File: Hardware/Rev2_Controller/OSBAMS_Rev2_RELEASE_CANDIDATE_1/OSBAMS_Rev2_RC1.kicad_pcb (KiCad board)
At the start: 4 copper layers, 100 x 90 mm, 142 parts, among them J1 12V_IN, J2 ESTOP, J3 ARM, J4 K1_COIL, J5 SHUNT_KELVIN, J6 PACK_SENSE, J7 TEMP_PROBE, J8 USB-C HOST, J9 SWD, Q1 IRLML0060, SW1 RESET, U1 STM32L476RGT6, U10 USBLC6-2SC6, U2 INA228, U3 LMR14006Y, U4 VO610A-1, U5 VO610A-1, U6 CP2102N, U7 ISO7721, U9 USBLC6-2SC6

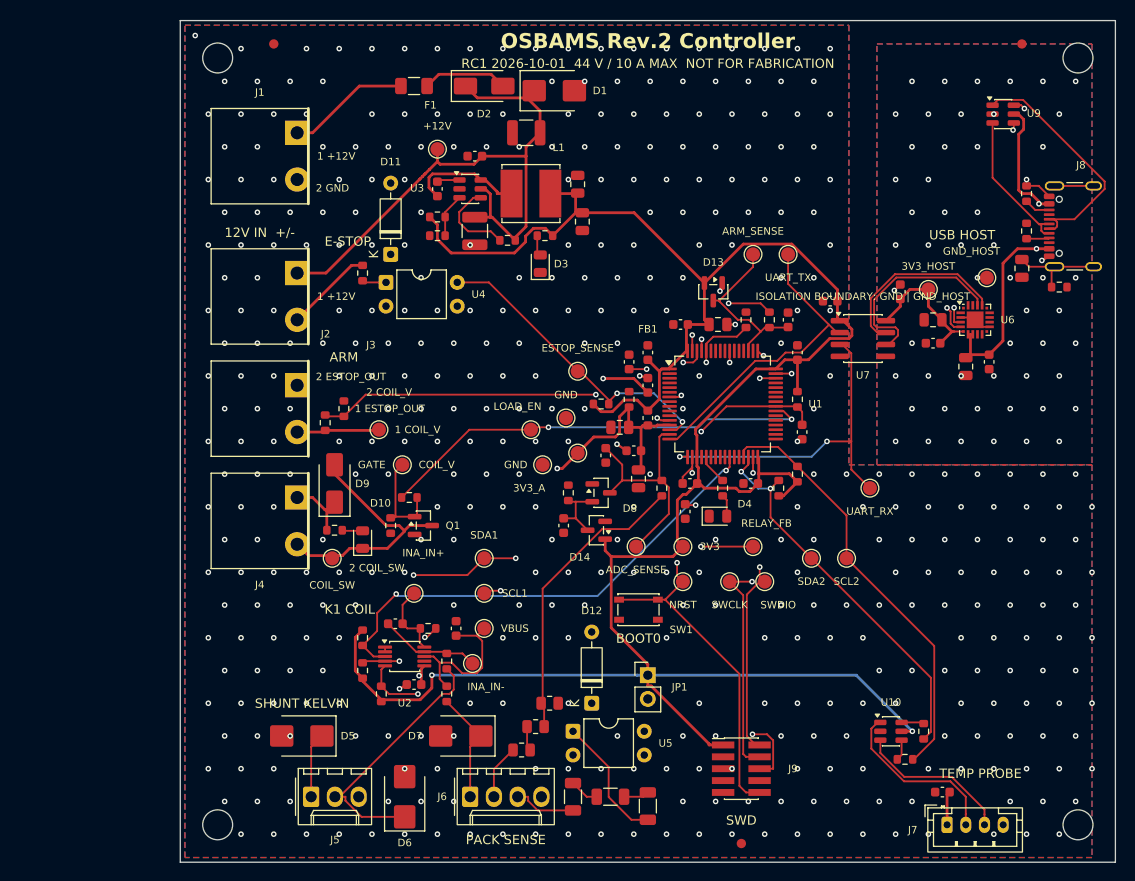
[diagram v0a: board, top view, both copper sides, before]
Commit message: RC1: EB21A-02-C footprint verified against the Adam Tech drawing (rev B); J1-J4 re-placed, board re-routed
Hole 1.30 mm, body 10.6 x 8.5 mm, wire entry toward the board edge; VERIFY_MECHANICAL_DRAWING removed
for this part only. ERC 0; DRC: 0 electrical, 4 silkscreen warnings, 0 unconnected.

Co-Authored-By: Claude Sonnet 5.5 <noreply@anthropic.com>
Claude-Session: https://claude.ai/code/session_01HV1TCrYnLTcNjmYdFqCPLo
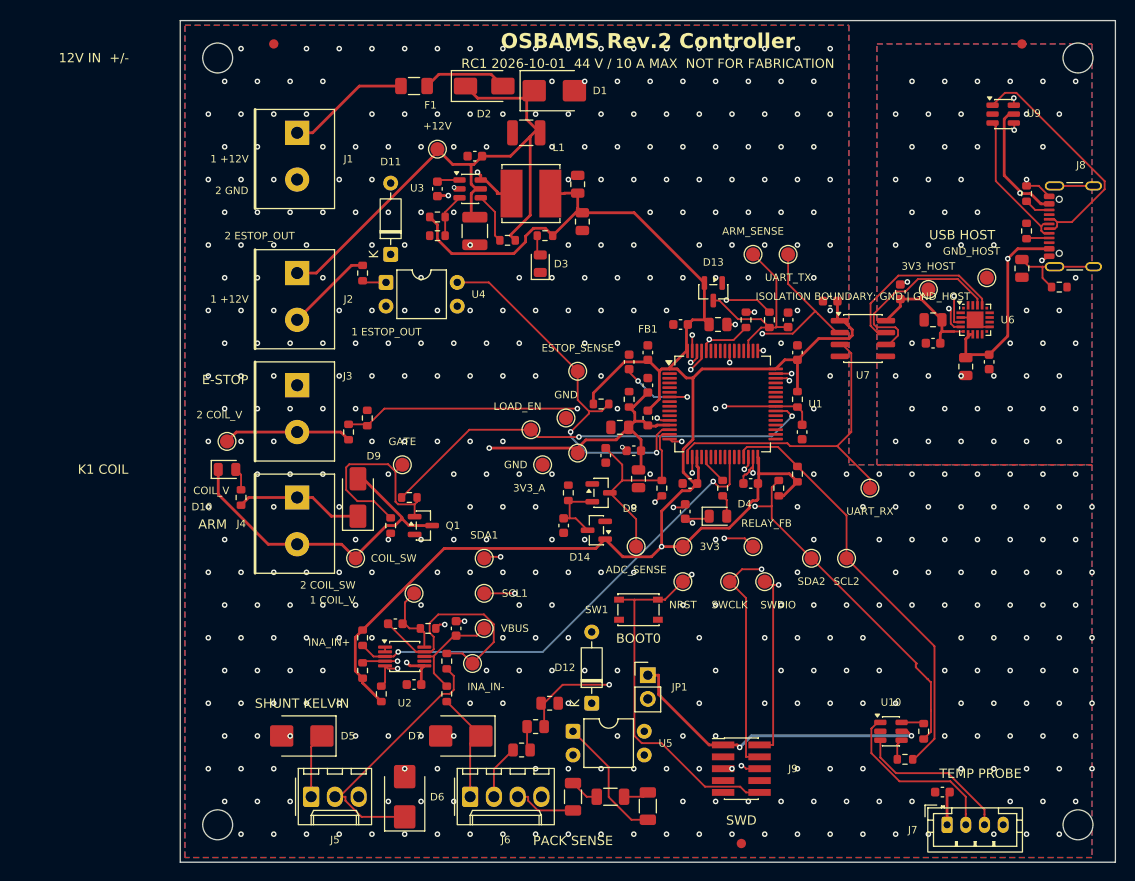
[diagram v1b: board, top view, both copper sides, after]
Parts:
- J1, J2, J3, J4: footprint OSBAMS_Rev2:EB21A-02-C_PROVISIONAL -> OSBAMS_Rev2:EB21A-02-C
- moved D10 16.3 mm to (105.0, 108.0), turned to 0 degrees
- moved TP16 16.3 mm to (105.0, 105.0)
- moved R23 10.6 mm to (106.5, 111.0), turned to 90 degrees
- moved D9 2.92 mm to (119.0, 111.0)
- moved R30 2.69 mm to (118.0, 104.0)
- moved R31 2.69 mm to (120.0, 102.5)
- moved TP15 2.50 mm to (118.8, 117.5)
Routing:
- net INA_INN: track 10.8 -> 25.2 mm
- net +3V3: track 272.4 -> 259.7 mm, vias 2 -> 3
- net GATE: track 10.6 -> 22.7 mm
- net COIL_V: track 22.9 -> 34.4 mm
- net 3V3_A: track 70.5 -> 61.7 mm, vias 3 -> 2
- net COIL_SW: track 28.5 -> 37.0 mm
- net NRST: track 61.7 -> 68.6 mm
- net INA_VBUS: track 17.0 -> 11.4 mm
- net ESTOP_SENSE: track 43.8 -> 49.0 mm
- net SCL1: track 63.8 -> 58.7 mm
- net SDA1: track 58.7 -> 53.9 mm, vias 4 -> 3
- net UART_TX_MCU: track 32.9 -> 37.5 mm, vias 0 -> 2
- net BUCK_EN: track 9.19 -> 5.39 mm
- net VBUS_USB: track 39.3 -> 42.8 mm
- net ARM_SENSE: track 18.7 -> 22.0 mm
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
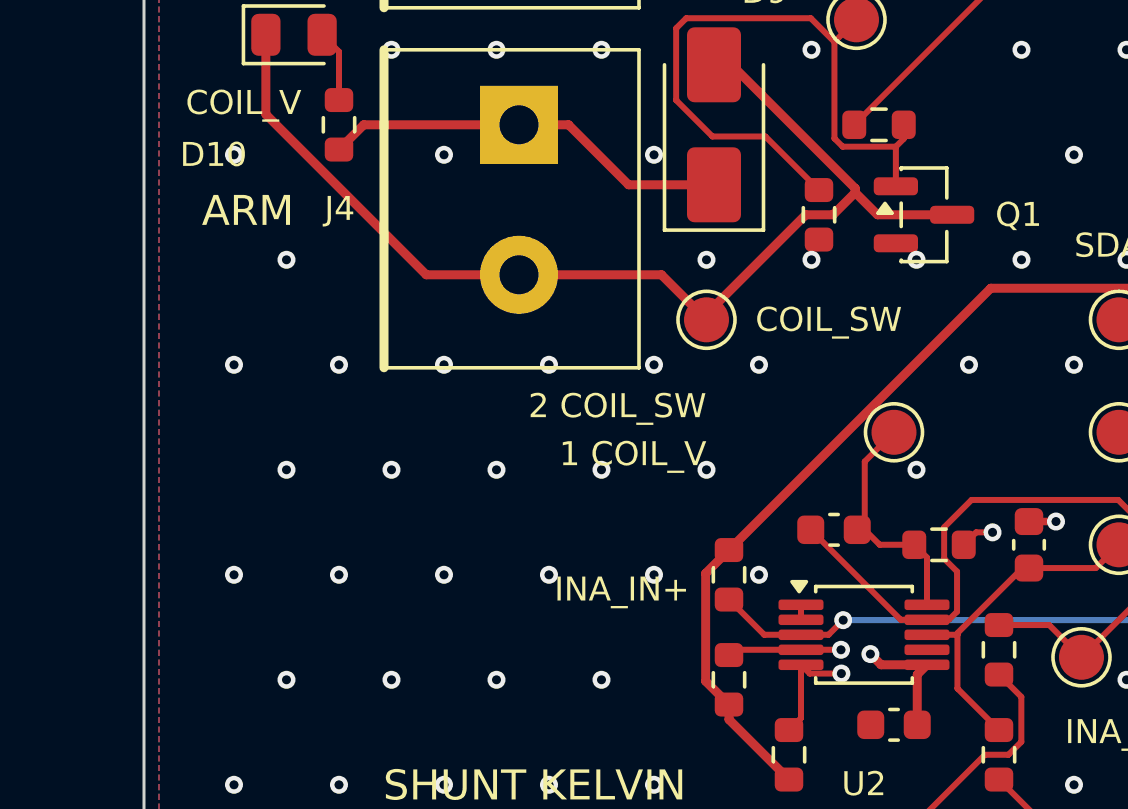
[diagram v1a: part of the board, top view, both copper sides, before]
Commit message: RC1: reconcile user-relayed manufacturer data (USER_RELAYED_MANUFACTURER)
- audit report MANUFACTURER_DATA_RECONCILIATION.md; INA228/STM32/IRLML0060/LMR14006Y/CP2102N/VO610A/TC74 pin maps match the relayed data
- ISO7721 pin-direction conflict left unresolved (needs the TI pin diagram); CP2102N VBUS reference connection open
- LMR14006Y: 95 ns TON_MIN analysis (15 V marginal, 24.4 V below TON_MIN); 1.5SMBJ48A vs INA228 85 V clamp-vs-current analysis
- firmware: INA228 IMAX 30 A -> 20 A (SHUNT_CAL 1250) + test
- fix: TC74 probe PCB had been left unrouted by the schematic step; re-routed, DRC 0; schematic step no longer rebuilds it

Co-Authored-By: Claude Sonnet 5.5 <noreply@anthropic.com>
Claude-Session: https://claude.ai/code/session_01HV1TCrYnLTcNjmYdFqCPLo
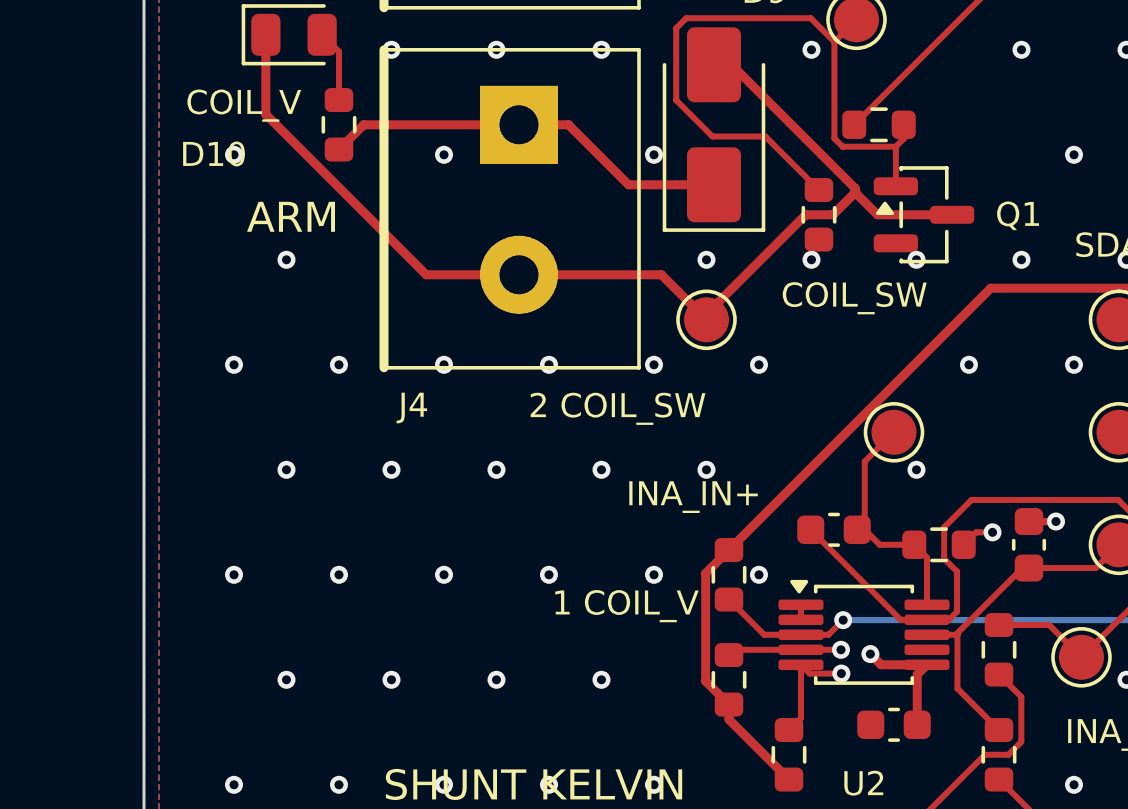
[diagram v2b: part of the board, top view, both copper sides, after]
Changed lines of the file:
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@@
 			)
 		)
-		(property "Evidence" "UNVERIFIED"
+		(property "Evidence" "USER_RELAYED_MANUFACTURER"
 			(at 0 0 0)
 			(layer "F.Fab")
@@
 		(tags "EB21A terminal block 5.00mm")
 		(property "Reference" "J4"
-			(at -5.975001 2.8 0)
+			(at -3.5125 9.360142 0)
 			(layer "F.SilkS")
 			(effects
@@
 			)
 		)
-		(property "Evidence" "UNVERIFIED"
+		(property "Evidence" "USER_RELAYED_MANUFACTURER"
 			(at 0 0 0)
 			(layer "F.Fab")
@@
 			)
 		)
-		(property "Evidence" "UNVERIFIED"
+		(property "Evidence" "USER_RELAYED_MANUFACTURER"
 			(at 0 0 0)
 			(layer "F.Fab")
@@
 			)
 		)
-		(property "Evidence" "USER_RELAYED_MANUFACTURER"
+		(property "Evidence" "UNVERIFIED"
 			(at 0 0 0)
 			(layer "F.Fab")
@@
 	)
 	(gr_text "INA_IN+"
-		(at 115.928383 126.4875 0)
+		(at 118.3225 123.310991 0)
 		(layer "F.SilkS")
 		(effects
@@
 	)
 	(gr_text "COIL_SW"
-		(at 122.825 117.5 0)
+		(at 123.6775 116.689008 0)
 		(layer "F.SilkS")
 		(effects
@@
 		)
 	)
-	(gr_text "2 COIL_SW"
-		(at 118.75 120.375 0)
+	(gr_text "1 COIL_V"
+		(at 118.49974 126.9525 0)
 		(layer "F.SilkS")
 		(effects
@@
 		)
 	)
-	(gr_text "1 COIL_V"
-		(at 118.75 121.975 0)
+	(gr_text "2 COIL_SW"
+		(at 118.75 120.375 0)
 		(layer "F.SilkS")
 		(effects
@@
 	)
 	(gr_text "ARM"
-		(at 105 113.875 0)
+		(at 106.5 114.104999 0)
 		(layer "F.SilkS")
 		(effects

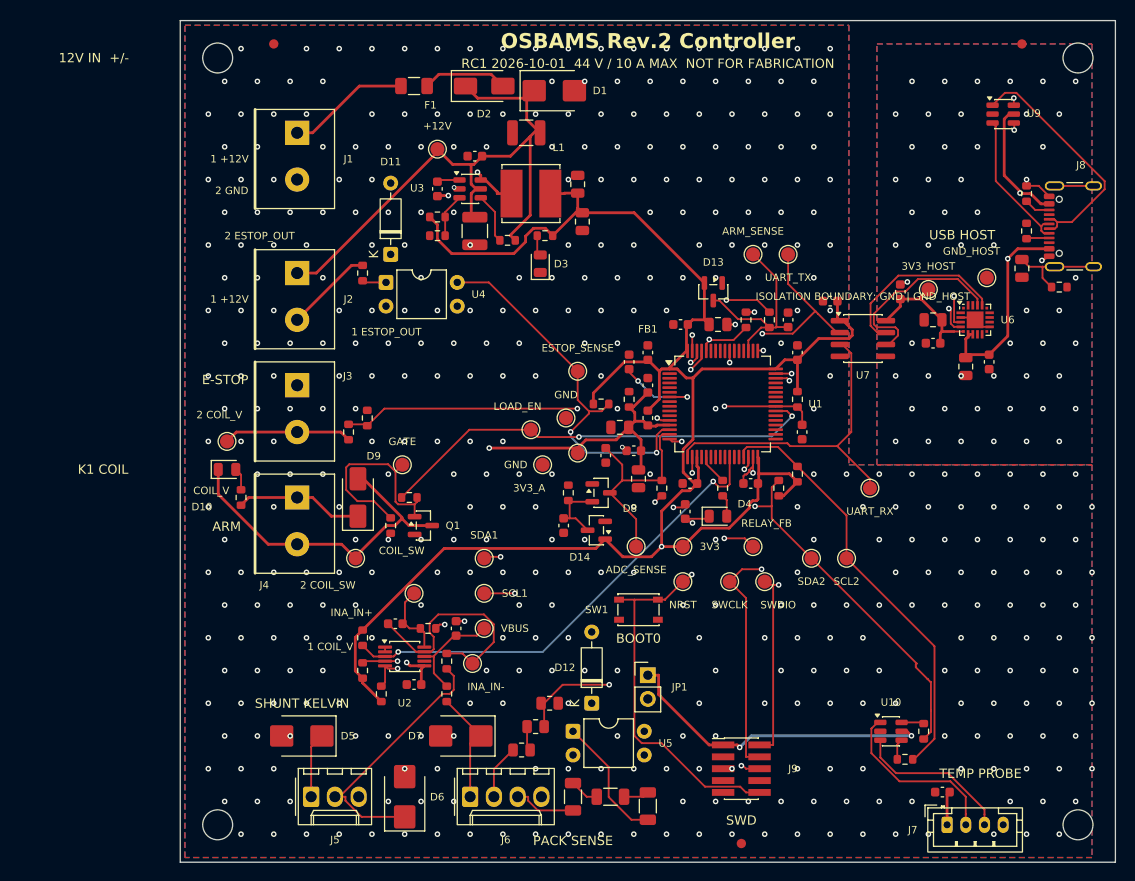
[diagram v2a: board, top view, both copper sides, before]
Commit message: RC1.1: ISO7721 pinout fix, CP2102N VBUS divider/RSTb pull-up/VDD bypass, datasheets read locally
- ISO7721 symbol corrected to the TI D/DWV table (2 OUTA, 3 INB, 6 OUTB, 7 INA); UART nets reassigned and re-routed
- CP2102N: VBUS 22.1k/47.5k divider (R38/R39), 1k RSTb pull-up (R40), VDD bypass 4.7uF (C22) per the datasheet
- ISO7721, CP2102N, SRN6045TA datasheets committed as evidence and marked VERIFIED_LOCAL; SRN6045TA-100M inductor closed
- isolation check script/report (3.0 mm in the ISO7721 area, 0.25 mm elsewhere); docs corrected (netclass clearances)
- board re-placed and re-routed: ERC 0, DRC 0 electrical (3 silkscreen warnings), netlist 0 mismatches

Co-Authored-By: Claude Sonnet 5.5 <noreply@anthropic.com>
Claude-Session: https://claude.ai/code/session_01HV1TCrYnLTcNjmYdFqCPLo
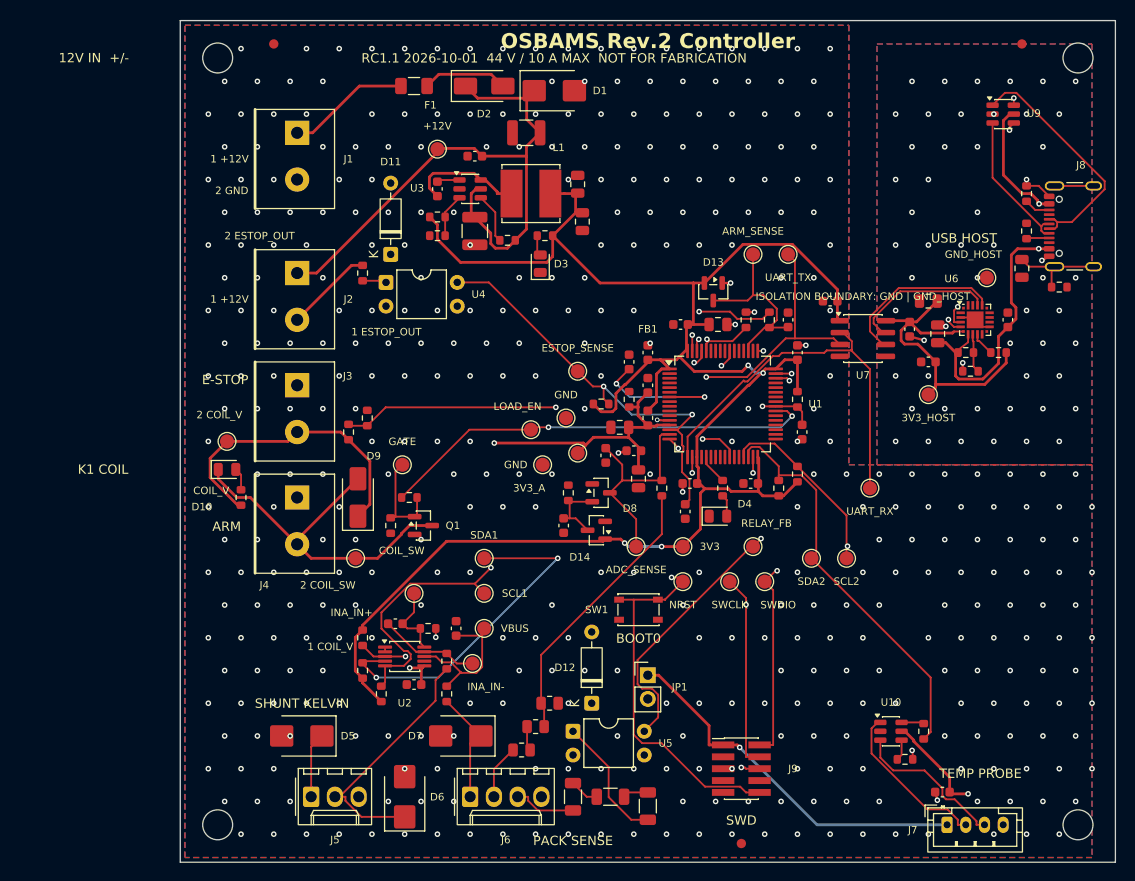
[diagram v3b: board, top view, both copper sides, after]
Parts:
- added R38: 22.1k, Resistor_SMD:R_0603_1608Metric, F.Cu at (184.0, 95.5)
- added R39: 47.5k, Resistor_SMD:R_0603_1608Metric, F.Cu at (184.5, 97.5)
- added R40: 1k, Resistor_SMD:R_0603_1608Metric, F.Cu at (187.5, 95.5)
- C22: value 1uF -> 4.7uF
- moved TP27 11.2 mm to (180.0, 100.0)
- moved C21 4.92 mm to (188.5, 92.0), turned to 90 degrees
- moved C20 4.61 mm to (181.0, 93.5), turned to 90 degrees
- moved C25 4.12 mm to (178.0, 93.0), turned to -90 degrees
- moved C22 2.06 mm to (180.0, 90.0)
- moved C23 2.06 mm to (180.0, 96.5)
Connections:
- U6 pad 8: VBUS_USB -> CP_VBUS_SENSE
- U6 pad 9: (no net) -> CP_RSTB
- U7 pad 2: UART_TX_MCU -> UART_RX_MCU
- U7 pad 3: UART_RX_MCU -> UART_TX_MCU
- U7 pad 6: UART_TX_HOST -> UART_RX_HOST
- U7 pad 7: UART_RX_HOST -> UART_TX_HOST
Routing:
- net 3V3_HOST: track 14.5 -> 33.2 mm
- net INA_INN: track 25.2 -> 10.8 mm
- net SDA1: track 53.9 -> 68.3 mm
- net GATE: track 22.7 -> 10.6 mm
- net +3V3: track 259.7 -> 271.7 mm, vias 3 -> 6
- net NRST: track 68.6 -> 76.5 mm
- net UART_RX_MCU: track 35.3 -> 41.8 mm
- net COIL_V: track 34.4 -> 39.6 mm
- net INA_VBUS: track 11.4 -> 16.3 mm
- net VBUS_USB: track 42.8 -> 47.7 mm
- net UART_TX_HOST: track 20.4 -> 15.6 mm
- net CP_VBUS_SENSE: track 0.00 -> 4.19 mm
- net ESTOP_SENSE: track 49.0 -> 45.0 mm, vias 3 -> 2
- net GND: track 18.5 -> 14.9 mm, vias 417 -> 404
- net RELAY_FB: track 51.7 -> 48.4 mm
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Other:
- board text added: "RC1.1 2026-10-01 44 V / 10 A MAX NOT FOR FABRICATION"
- board text removed: "RC1 2026-10-01 44 V / 10 A MAX NOT FOR FABRICATION"

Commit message: RC1.2: pack-sense surge resistors, isolation/clearance rules, buck envelope, evidence classification, no shipped Gerbers
- R41 47R (PACK_INA) and R42/R43 10R (Kelvin lines) upstream of the 1.5SMBJ48A diodes; credible-transient analysis with simulation (PASS)
- custom DRC rules: host-to-controller >= 1.0 mm on every layer, INA228 fine-pitch exemption; pack-level class 0.2 mm (IPC-2221B B4 basis)
- isolation audit per layer with coordinates; XDR 12.0 V / max continuous input 14.4 V; IRLML0060 margin estimate + mandatory first-article checks
- board re-routed: ERC 0, DRC 0, unconnected 0, netlist 0 mismatches (403 pads); silkscreen warnings fixed
- script-generated Gerbers/drills removed from the package; BOM adds qty for 5 boards and MPN suffix status; new evidence-risk, connector-check and pre-PCBWay checklist documents

Co-Authored-By: Claude Sonnet 5.5 <noreply@anthropic.com>
Claude-Session: https://claude.ai/code/session_01HV1TCrYnLTcNjmYdFqCPLo
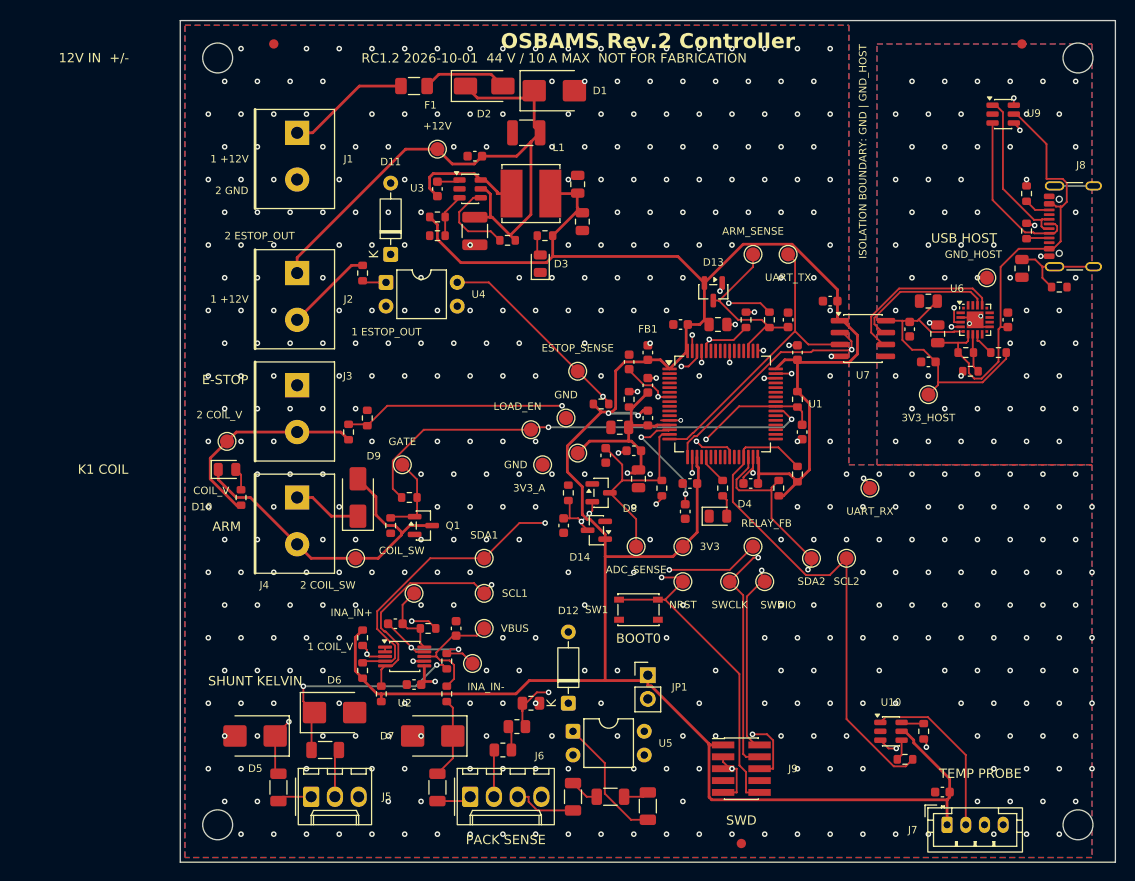
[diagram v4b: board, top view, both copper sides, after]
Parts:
- added R41: 47, Resistor_SMD:R_1206_3216Metric, F.Cu at (127.5, 142.0)
- added R42: 10, Resistor_SMD:R_1206_3216Metric, F.Cu at (110.5, 142.0)
- added R43: 10, Resistor_SMD:R_1206_3216Metric, F.Cu at (115.5, 138.0)
- moved D6 11.7 mm to (116.5, 134.0), turned to 0 degrees
- moved D5 5.00 mm to (108.0, 136.5)
- moved D7 3.00 mm to (127.0, 136.5)
- moved D12 2.50 mm to (141.5, 133.0)
- moved R17 2.00 mm to (134.5, 138.0)
- moved R18 2.00 mm to (136.0, 135.5)
- moved R19 2.00 mm to (137.5, 133.0)
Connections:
- J5 pad 1: SHUNT_INP_RAW -> SHUNT_INP_CON
- J5 pad 2: SHUNT_INN_RAW -> SHUNT_INN_CON
- J6 pad 1: PACK_INA -> PACK_INA_CON
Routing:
- net NRST: track 76.5 -> 61.2 mm, vias 3 -> 2
- net GND: track 14.9 -> 26.9 mm, vias 404 -> 408
- net SCL2: track 45.6 -> 55.6 mm, vias 2 -> 0
- net INA_ALERT: track 50.7 -> 60.2 mm
- net RELAY_FB: track 48.4 -> 57.9 mm
- net +3V3: track 271.7 -> 280.7 mm, vias 6 -> 2
- net USB_DP_J: track 26.2 -> 17.6 mm
- net SDA1: track 68.3 -> 60.8 mm, vias 3 -> 2
- net 3V3_A: track 63.2 -> 55.9 mm
- net SHUNT_INN_CON: track 0.00 -> 5.18 mm
- net ESTOP_SENSE: track 45.0 -> 40.2 mm, vias 2 -> 3
- net GND_HOST: track 10.7 -> 6.21 mm, vias 55 -> 61
- net INA_INN: track 10.8 -> 15.0 mm, vias 0 -> 2
- net BUCK_EN: track 5.39 -> 9.19 mm
- net UART_TX_MCU: track 35.8 -> 32.1 mm, vias 2 -> 0
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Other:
- board text added: "RC1.2 2026-10-01 44 V / 10 A MAX NOT FOR FABRICATION"
- board text removed: "RC1.1 2026-10-01 44 V / 10 A MAX NOT FOR FABRICATION"
